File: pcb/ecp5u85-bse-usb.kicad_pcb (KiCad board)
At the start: 6 copper layers, 50 x 75 mm, 220 parts, among them J1 BSE-040-01-X-D-A, J2 BSE-040-01-X-D-A, J3 JTAG, J4 USB3_B_micro, J5 Barrel_Jack_Switch, Q1 Q_NMOS_GSD, Q2 ZXMC3A16DN8, U1 LFE5U-85F-6BG381, U2 SiT9120AC-2C2-25E100.000000X, U3 W25Q128JVP, U4 MT41K64M16TW-x, U5 ECMF02-4CMX8, U6 ECMF04-4HSWM10, U8 LTC4360-2, U9 LTM8051, Y1 30MHz

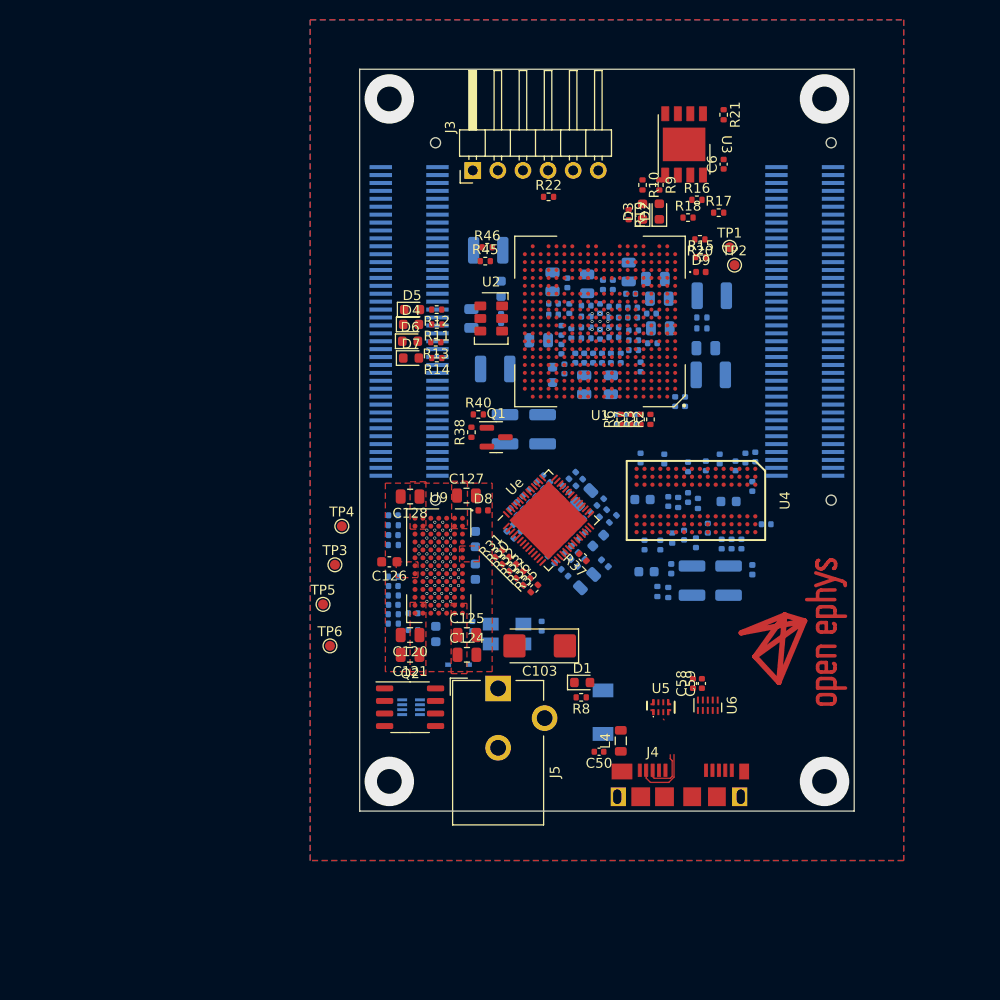
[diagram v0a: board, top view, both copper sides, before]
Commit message: Performed rough RAM routing
- Traces 25 mm long, all matched.
- No power routed yet but I want to confirm that FPGA pin remap before
going forward because I can probably make this work.
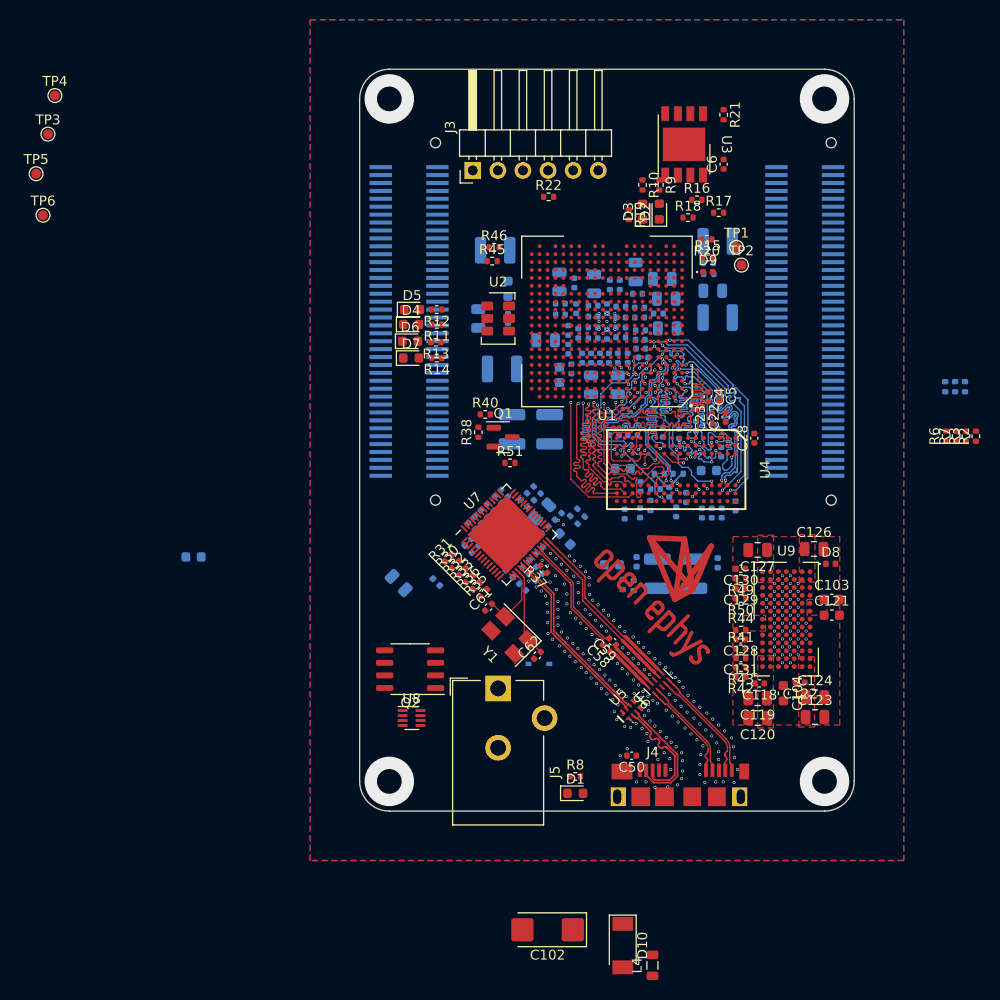
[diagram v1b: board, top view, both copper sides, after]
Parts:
- removed the C73 at (156.7, 83.4)
- added R51: 0, Resistor_SMD:R_0402_1005Metric, F.Cu at (144.2, 94.8)
- C103: renamed from C104; moved to F.Cu
- C104: renamed from C105; moved to F.Cu
- C118: renamed from C119; moved to F.Cu
- C121: renamed from C122; moved to F.Cu
- C122: renamed from C123; moved to F.Cu
- C125: renamed from C126; moved to B.Cu
- C128: renamed from C129; moved to F.Cu
- C129: renamed from C130; moved to F.Cu
- C130: renamed from C131; moved to F.Cu
- C131: renamed from C132; moved to F.Cu
- C15: value 100nF -> 10nF
- C22, C23, C28, C4, C5, C61, C62, D10, R41, R42, R43, R44, R49, R50, U8, Y1: moved to F.Cu
- moved TP4 52.3 mm to (98.2, 57.7)
- moved TP3 52.3 mm to (97.5, 61.6)
- moved TP6 52.3 mm to (97.0, 69.8)
- moved TP5 52.3 mm to (96.3, 65.6)
- moved C122 39.8 mm to (173.5, 117.0)
- moved C103 36.5 mm to (176.7, 108.6), turned to 0 degrees
- moved C121 36.3 mm to (176.7, 110.2), turned to 0 degrees
- moved C123 35.7 mm to (175.0, 120.5)
- moved C124 35.7 mm to (175.0, 118.5)
- moved C119 35.7 mm to (169.2, 118.6)
- moved C120 35.7 mm to (169.2, 120.6)
- moved C104 35.6 mm to (171.8, 118.1)
- moved C127 35.6 mm to (169.2, 103.6)
- moved C128 35.6 mm to (167.5, 112.7)
- moved C129 35.6 mm to (167.5, 107.5)
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- renumbered C101 to C100, C102 to C101, C103 to C102, C106 to C105, C107 to C106, C108 to C107, C109 to C108, C110 to C109, C111 to C110, C112 to C111, C113 to C112, C114 to C113, C115 to C114, C116 to C115, C117 to C116, C118 to C117, C120 to C119, C121 to C120, C124 to C123, C125 to C124, C127 to C126, C128 to C127, C67 to C66, C68 to C67, C69 to C68, C70 to C69, C71 to C70, C74 to C73, C75 to C74, C76 to C75, C77 to C76, C78 to C77, C79 to C78, C80 to C79, C81 to C80, C82 to C81, C83 to C82, C84 to C83, C85 to C84, C86 to C85, C87 to C86, C88 to C87, C89 to C88, C90 to C89, C91 to C90, C92 to C91, C93 to C92, C94 to C93, C95 to C94, C96 to C95, C97 to C96, C98 to C97, C99 to C98, C100 to C99, Ue to U7
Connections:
- net Net-(C58-Pad2) renamed /FTDI/TOD-
- net Net-(C59-Pad2) renamed /FTDI/TOD+
- net Net-(J4-Pad2) renamed /FTDI/D_{Con}-
- net Net-(J4-Pad3) renamed /FTDI/D_{Con}+
- net Net-(U5-Pad6) renamed /FTDI/D_{IC}-
- net Net-(U5-Pad7) renamed /FTDI/D_{IC}+
- C58 pad 1: Net-(C58-Pad1) -> /FTDI/SSTX_{IC}-
- C59 pad 1: Net-(C59-Pad1) -> /FTDI/SSTX_{IC}+
- J4 pad 10: Net-(J4-Pad10) -> /FTDI/SSRX_{Con}+
- J4 pad 6: Net-(J4-Pad6) -> /FTDI/SSTX_{Con}-
- J4 pad 7: Net-(J4-Pad7) -> /FTDI/SSTX_{Con}+
- J4 pad 9: Net-(J4-Pad9) -> /FTDI/SSRX_{Con}-
- U1 pad A3: /FPGA/RAM_DQ6 -> /FPGA/RAM_LDM
- U1 pad A4: /FPGA/RAM_DQ0 -> /FPGA/RAM_DQ1
- U1 pad A5: /FPGA/RAM_DQ1 -> /FPGA/RAM_DQ7
- U1 pad A6: /FPGA/RAM_A0 -> /FPGA/RAM_A5
- U1 pad A7: /FPGA/RAM_A12 -> /FPGA/RAM_BA0
- U1 pad A8: /FPGA/RAM_BA0 -> /FPGA/RAM_A2
- U1 pad B1: /FPGA/RAM_DQ9 -> /FPGA/RAM_UDM
- U1 pad B3: /FPGA/RAM_DQ7 -> /FPGA/RAM_DQ2
- U1 pad B4: /FPGA/RAM_DQ5 -> /FPGA/RAM_DQ3
- U1 pad B5: /FPGA/RAM_DQ2 -> /FPGA/RAM_DQ5
- U1 pad B6: /FPGA/RAM_A1 -> /FPGA/RAM_A9
- U1 pad B8: /FPGA/RAM_A11 -> /FPGA/RAM_BA2
- U1 pad C11: /FPGA/~{FT_WAKEUP} -> Net-(R51-Pad2)
- U1 pad C2: /FPGA/RAM_DQ10 -> /FPGA/RAM_DQ9
- U1 pad C3: /FPGA/RAM_LDM -> /FPGA/RAM_DQ0
- U1 pad C4: /FPGA/RAM_DQ4 -> /FPGA/RAM_DQ6
- U1 pad C5: /FPGA/RAM_DQ3 -> /FPGA/RAM_DQ4
- U1 pad C6: /FPGA/RAM_A6 -> /FPGA/RAM_A7
- U1 pad C7: /FPGA/RAM_A7 -> /FPGA/RAM_A0
- U1 pad D1: /FPGA/RAM_DQ13 -> /FPGA/RAM_DQ15
- U1 pad D2: /FPGA/RAM_DQ12 -> /FPGA/RAM_UDQS+
- U1 pad D3: /FPGA/RAM_ODT -> /FPGA/~{RAM_CS}
- U1 pad D7: /FPGA/RAM_A5 -> /FPGA/RAM_A12
- U1 pad D8: /FPGA/RAM_A9 -> /FPGA/RAM_BA1
- U1 pad D9: /FPGA/RAM_BA1 -> /FPGA/RAM_A8
- U1 pad E1: /FPGA/RAM_DQ14 -> /FPGA/RAM_UDQS-
- U1 pad E2: /FPGA/~{RAM_WE} -> /FPGA/RAM_ODT
- U1 pad E6: /FPGA/RAM_A2 -> /FPGA/RAM_A1
- U1 pad E8: /FPGA/RAM_A8 -> /FPGA/RAM_A11
- U1 pad E9: /FPGA/RAM_BA2 -> /FPGA/RAM_A6
- U1 pad F2: /FPGA/~{RAM_RAS} -> /FPGA/~{RAM_CAS}
- U1 pad F3: /FPGA/~{RAM_CAS} -> /FPGA/~{RAM_RAS}
- U1 pad G3: /FPGA/~{RAM_CS} -> /FPGA/~{RAM_WE}
- U1 pad G5: /FPGA/RAM_UDQS- -> /FPGA/RAM_DQ13
- U1 pad H3: /FPGA/RAM_DQ15 -> /FPGA/RAM_DQ14
- U1 pad H4: /FPGA/RAM_UDQS+ -> /FPGA/RAM_DQ10
- U1 pad H5: /FPGA/RAM_UDM -> /FPGA/RAM_DQ12
- U6 pad 1: Net-(U6-Pad1) -> /FTDI/SSTX_{Con}-
- U6 pad 10: Net-(J4-Pad10) -> /FTDI/SSTX_{IC}-
- U6 pad 2: Net-(U6-Pad2) -> /FTDI/SSTX_{Con}+
- U6 pad 4: Net-(C59-Pad1) -> /FTDI/SSRX_{Con}-
- U6 pad 5: Net-(C58-Pad1) -> /FTDI/SSRX_{Con}+
- U6 pad 6: Net-(J4-Pad6) -> /FTDI/SSRX_{IC}+
- U6 pad 7: Net-(J4-Pad7) -> /FTDI/SSRX_{IC}-
- U6 pad 9: Net-(J4-Pad9) -> /FTDI/SSTX_{IC}+
- U7 pad 27: Net-(U6-Pad2) -> /FTDI/SSRX_{IC}-
- U7 pad 28: Net-(U6-Pad1) -> /FTDI/SSRX_{IC}+
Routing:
- net /FPGA/RAM_A6: track 0.00 -> 25.4 mm, vias 0 -> 2
- net /FPGA/RAM_CK+: track 0.00 -> 25.1 mm, vias 0 -> 2
- net /FPGA/RAM_CK-: track 0.00 -> 24.8 mm, vias 0 -> 2
- net /FPGA/RAM_A2: track 0.00 -> 24.7 mm, vias 0 -> 1
- net /FPGA/RAM_DQ3: track 0.00 -> 24.7 mm, vias 0 -> 2
- net /FPGA/RAM_LDQS+: track 0.00 -> 24.0 mm, vias 0 -> 2
- net /FPGA/RAM_BA2: track 0.00 -> 23.7 mm, vias 0 -> 2
- net /FPGA/RAM_A0: track 0.00 -> 23.7 mm, vias 0 -> 2
- net /FPGA/RAM_A4: track 0.00 -> 23.6 mm, vias 0 -> 2
- net /FPGA/~{RAM_CAS}: track 0.00 -> 23.6 mm, vias 0 -> 2
- net /FPGA/RAM_DQ5: track 0.00 -> 23.5 mm, vias 0 -> 2
- net /FPGA/~{RAM_RAS}: track 0.00 -> 23.5 mm, vias 0 -> 2
- net /FPGA/RAM_A3: track 0.00 -> 23.5 mm, vias 0 -> 2
- net /FPGA/RAM_BA0: track 0.00 -> 23.5 mm, vias 0 -> 2
- net /FPGA/RAM_A12: track 0.00 -> 23.5 mm, vias 0 -> 2
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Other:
- outline, holes or cut-outs redrawn

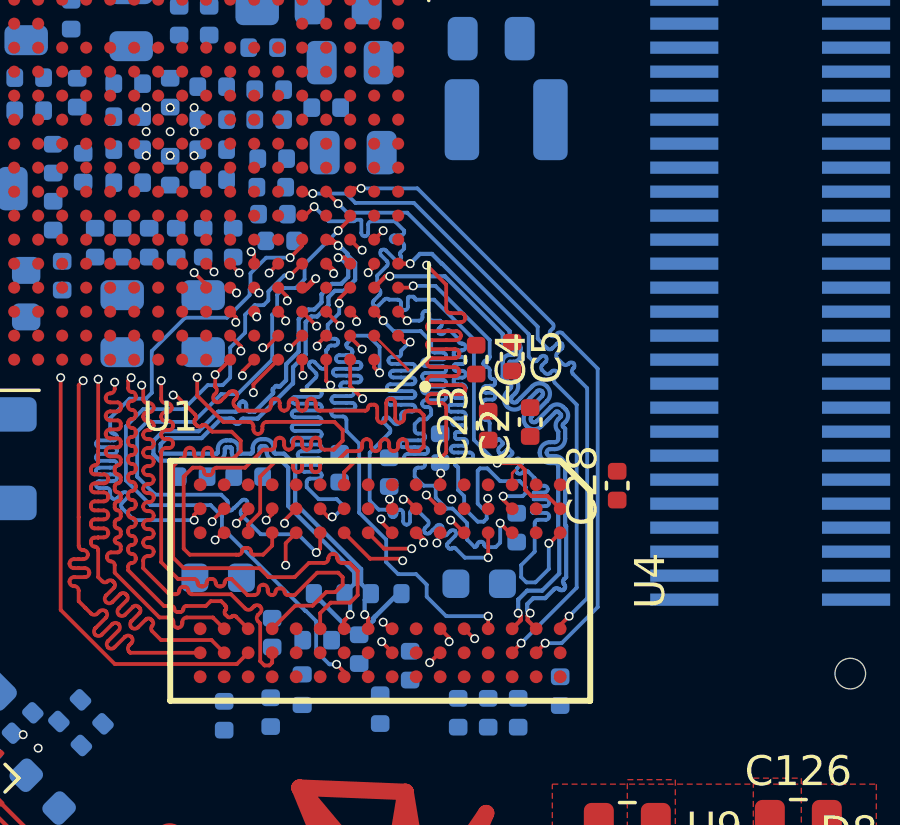
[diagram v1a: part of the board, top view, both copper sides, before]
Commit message: Return RAM UDQS signals to dedicated FPGA pin
- J1.2 moved to ground instead of RAM_VDD
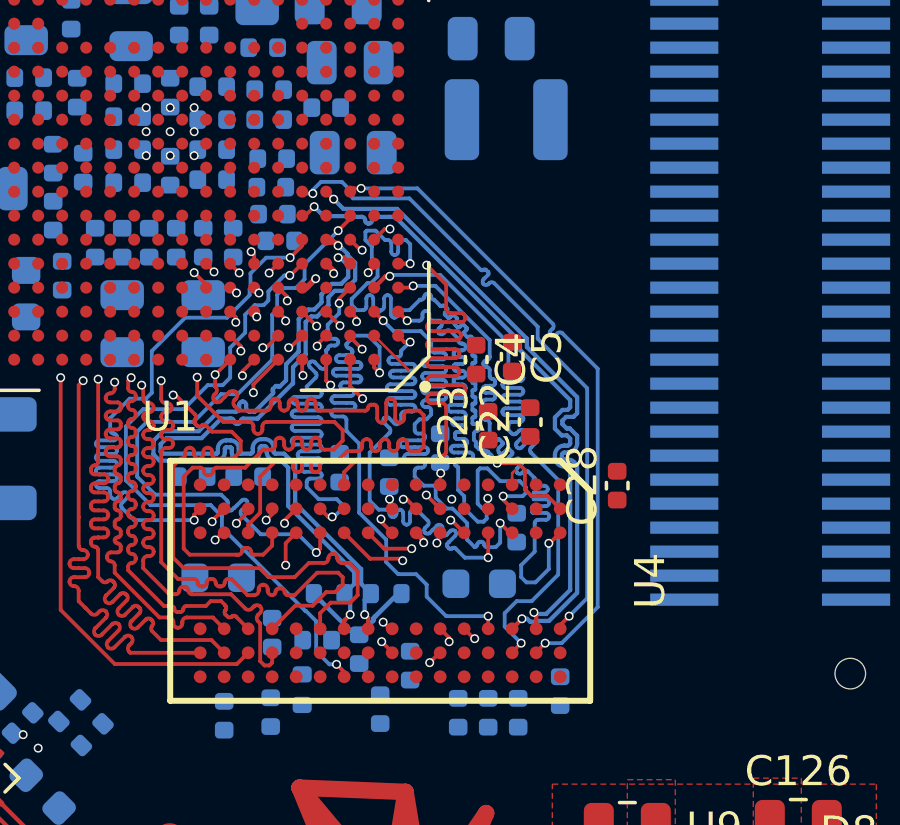
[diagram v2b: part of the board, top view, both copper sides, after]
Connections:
- J1 pad 2: RAM_VDD -> GND
- U1 pad D2: /FPGA/RAM_UDQS+ -> /FPGA/RAM_DQ10
- U1 pad E1: /FPGA/RAM_UDQS- -> /FPGA/RAM_DQ13
- U1 pad G5: /FPGA/RAM_DQ13 -> /FPGA/RAM_UDQS-
- U1 pad H4: /FPGA/RAM_DQ10 -> /FPGA/RAM_UDQS+
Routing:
- net /FPGA/RAM_DQ4: track 12.6 -> 23.3 mm
- net /FPGA/RAM_DQ10: track 21.9 -> 24.1 mm
- net /FPGA/RAM_DQ13: track 21.7 -> 23.6 mm
